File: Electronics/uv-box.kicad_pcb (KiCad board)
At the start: 2 copper layers, 172.7 x 50.8 mm, 73 parts, among them P1 CONN_2

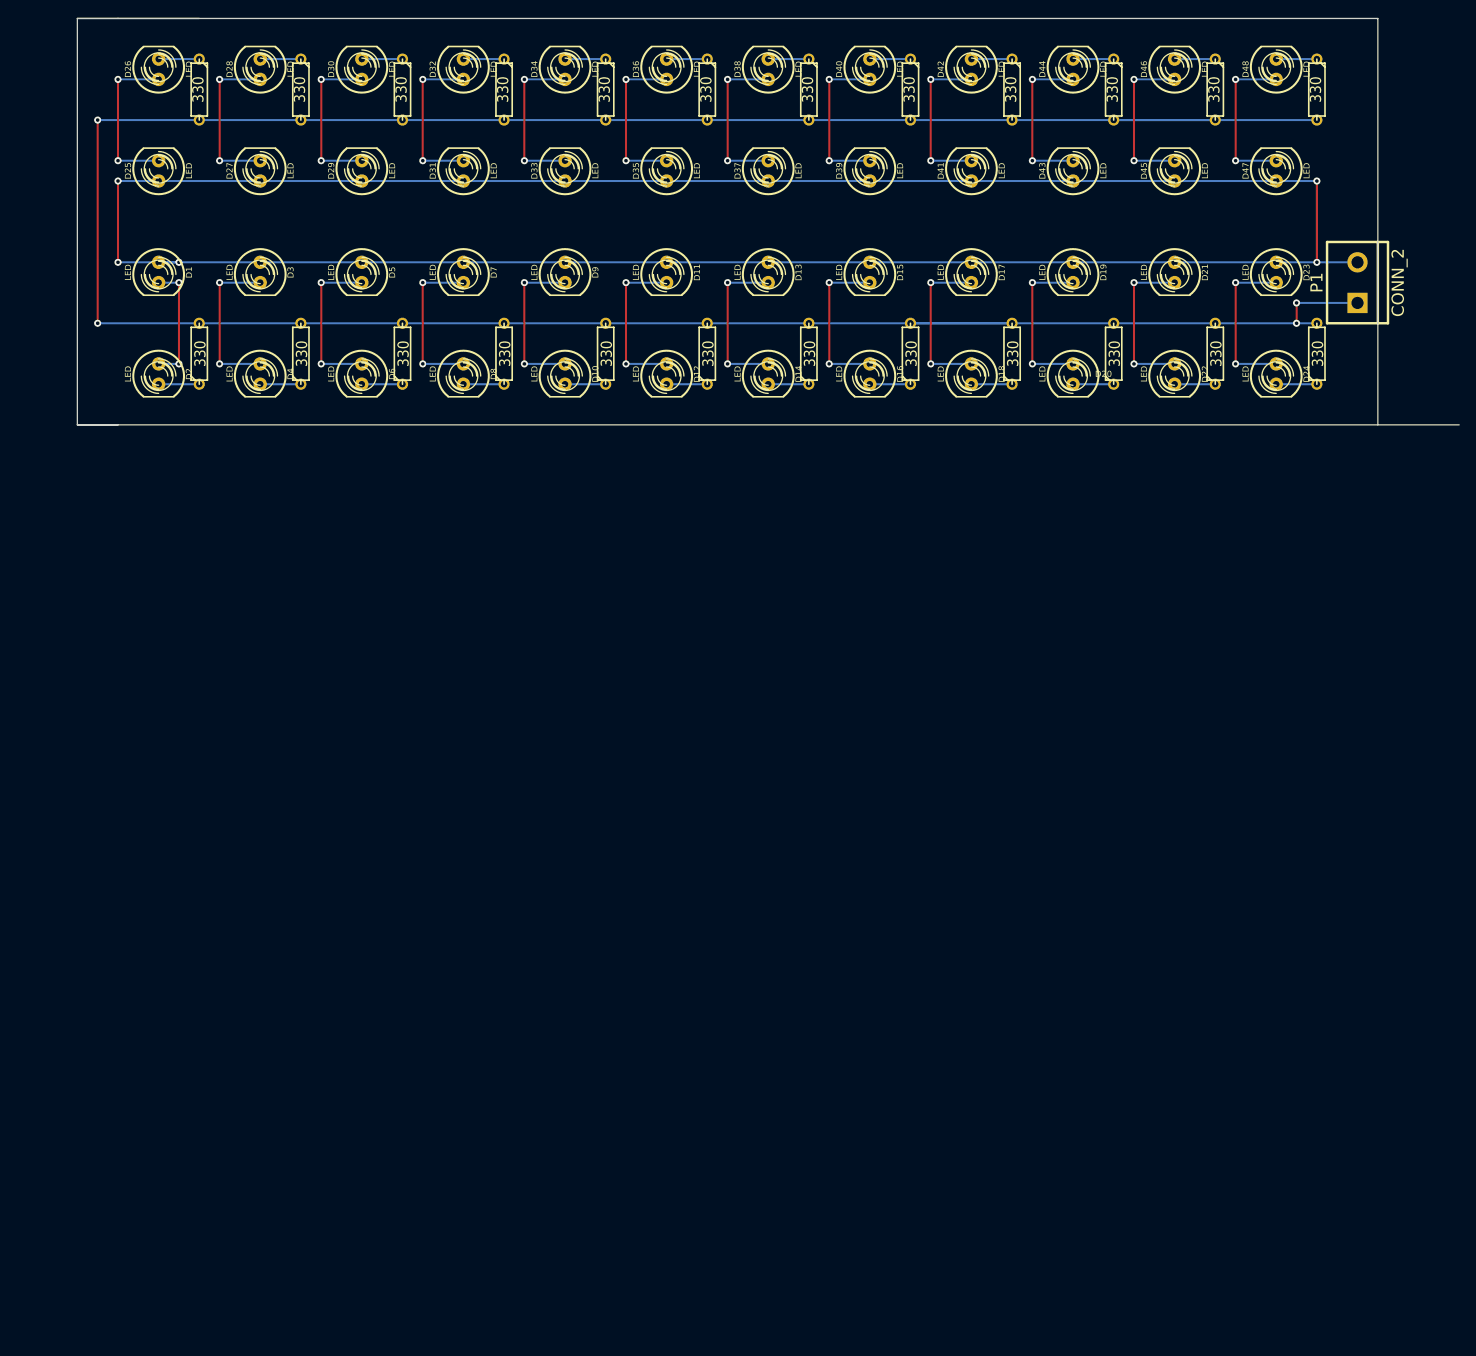
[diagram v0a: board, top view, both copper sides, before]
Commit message: 84 LED per panel.
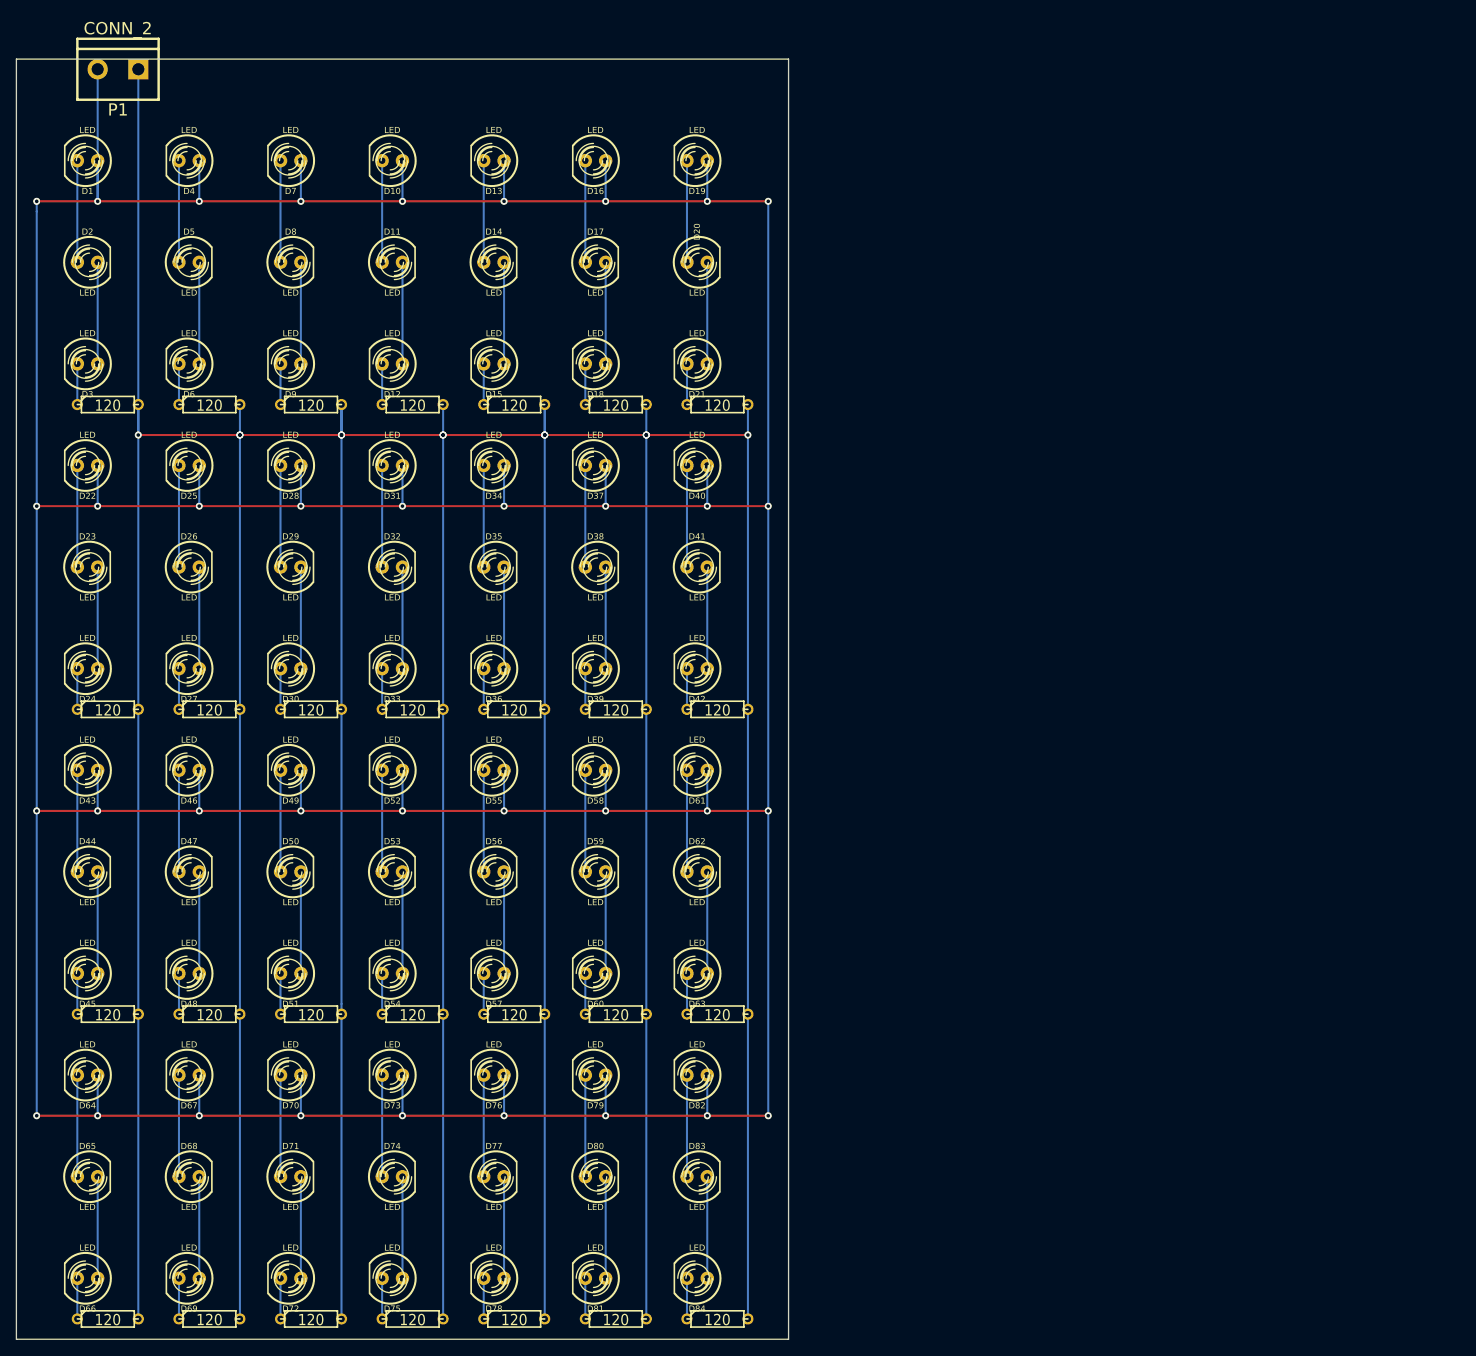
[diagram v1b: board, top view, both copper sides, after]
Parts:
- added D49: LED, LED-5MM, F.Cu at (123.2, 114.3)
- added D50: LED, LED-5MM, F.Cu at (123.2, 127.0)
- added D51: LED, LED-5MM, F.Cu at (123.2, 139.7)
- added D52: LED, LED-5MM, F.Cu at (135.9, 114.3)
- added D53: LED, LED-5MM, F.Cu at (135.9, 127.0)
- added D54: LED, LED-5MM, F.Cu at (135.9, 139.7)
- added D55: LED, LED-5MM, F.Cu at (148.6, 114.3)
- added D56: LED, LED-5MM, F.Cu at (148.6, 127.0)
- added D57: LED, LED-5MM, F.Cu at (148.6, 139.7)
- added D58: LED, LED-5MM, F.Cu at (161.3, 114.3)
- added D59: LED, LED-5MM, F.Cu at (161.3, 127.0)
- added D60: LED, LED-5MM, F.Cu at (161.3, 139.7)
- added D61: LED, LED-5MM, F.Cu at (174.0, 114.3)
- added D62: LED, LED-5MM, F.Cu at (174.0, 127.0)
- added D63: LED, LED-5MM, F.Cu at (174.0, 139.7)
- added D64: LED, LED-5MM, F.Cu at (97.8, 152.4)
- added D65: LED, LED-5MM, F.Cu at (97.8, 165.1)
- added D66: LED, LED-5MM, F.Cu at (97.8, 177.8)
- added D67: LED, LED-5MM, F.Cu at (110.5, 152.4)
- added D68: LED, LED-5MM, F.Cu at (110.5, 165.1)
- added D69: LED, LED-5MM, F.Cu at (110.5, 177.8)
- added D70: LED, LED-5MM, F.Cu at (123.2, 152.4)
- added D71: LED, LED-5MM, F.Cu at (123.2, 165.1)
- added D72: LED, LED-5MM, F.Cu at (123.2, 177.8)
- added D73: LED, LED-5MM, F.Cu at (135.9, 152.4)
- added D74: LED, LED-5MM, F.Cu at (135.9, 165.1)
- added D75: LED, LED-5MM, F.Cu at (135.9, 177.8)
- added D76: LED, LED-5MM, F.Cu at (148.6, 152.4)
- added D77: LED, LED-5MM, F.Cu at (148.6, 165.1)
- added D78: LED, LED-5MM, F.Cu at (148.6, 177.8)
- added D79: LED, LED-5MM, F.Cu at (161.3, 152.4)
- added D80: LED, LED-5MM, F.Cu at (161.3, 165.1)
- added D81: LED, LED-5MM, F.Cu at (161.3, 177.8)
- added D82: LED, LED-5MM, F.Cu at (174.0, 152.4)
- added D83: LED, LED-5MM, F.Cu at (174.0, 165.1)
- added D84: LED, LED-5MM, F.Cu at (174.0, 177.8)
- added R25: 120, R3, F.Cu at (138.4, 182.9)
- added R26: 120, R3, F.Cu at (151.1, 182.9)
- added R27: 120, R3, F.Cu at (163.8, 182.9)
- added R28: 120, R3, F.Cu at (176.5, 182.9)
- R1, R10, R11, R12, R13, R14, R15, R16, R17, R18, R19, R2, R20, R21, R22, R23, R24, R3, R4, R5, R6, R7, R8, R9: value 330 -> 120
- moved R22 198.6 mm to (100.3, 182.9), turned to 0 degrees
- moved R23 198.6 mm to (113.0, 182.9), turned to 0 degrees
- moved R24 198.6 mm to (125.7, 182.9), turned to 0 degrees
- moved D48 176.8 mm to (110.5, 139.7), turned to 180 degrees
- moved D45 168.9 mm to (97.8, 139.7), turned to 180 degrees
- moved D47 161.7 mm to (110.5, 127.0), turned to 0 degrees
- moved D44 158.9 mm to (97.8, 127.0), turned to 0 degrees
- moved P1 157.2 mm to (101.6, 26.7), turned to 180 degrees
- moved D23 153.1 mm to (97.8, 88.9), turned to 0 degrees
- moved D24 153.1 mm to (97.8, 101.6), turned to 180 degrees
- moved D46 151.2 mm to (110.5, 114.3), turned to 180 degrees
- moved D43 144.2 mm to (97.8, 114.3), turned to 180 degrees
- moved D22 136.4 mm to (97.8, 76.2), turned to 180 degrees
- moved R15 121.3 mm to (100.3, 144.8), turned to 0 degrees
- moved R16 121.3 mm to (113.0, 144.8), turned to 0 degrees
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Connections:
- D10 pad 1: N-0000022 -> +12V
- D10 pad 2: N-000009 -> N-0000056
- D11 pad 1: +12V -> N-0000056
- D12 pad 2: N-000008 (its old number) -> N-0000054
- D14 pad 2: N-000007 -> N-0000058
- D15 pad 1: +12V -> N-0000058
- D15 pad 2: N-0000019 -> N-0000057
- D16 pad 1: N-0000019 -> +12V
- D16 pad 2: N-000006 -> N-0000062
- D17 pad 1: +12V -> N-0000062
- D18 pad 2: N-000005 -> N-0000060
- D2 pad 2: N-0000012 -> N-0000045
- D20 pad 2: N-000004 -> N-0000064
- D21 pad 1: +12V -> N-0000064
- D21 pad 2: N-0000016 -> N-0000063
- D22 pad 1: N-0000016 -> +12V
- D22 pad 2: N-000003 -> N-0000069
- D23 pad 1: +12V -> N-0000069
- D24 pad 2: N-000002 -> N-0000067
- D25 pad 1: N-0000041 -> +12V
- D26 pad 2: N-0000038 -> N-0000071
- D27 pad 1: N-0000041 -> N-0000071
- D27 pad 2: N-0000051 -> N-0000070
- D28 pad 1: N-0000051 -> +12V
- D28 pad 2: N-0000037 -> N-0000065
- D29 pad 1: N-0000041 -> N-0000065
- D3 pad 1: +12V -> N-0000045
- D3 pad 2: N-0000025 -> N-0000044
- D30 pad 2: N-0000036 -> N-0000073
- D31 pad 1: N-0000041 -> +12V
- D32 pad 2: N-0000035 -> N-0000077
- D33 pad 1: N-0000041 -> N-0000077
- D33 pad 2: N-0000040 -> N-0000076
- D34 pad 1: N-0000040 -> +12V
- D34 pad 2: N-0000034 -> N-0000081
- D35 pad 1: N-0000041 -> N-0000081
- D36 pad 2: N-0000033 -> N-0000079
- D37 pad 1: N-0000041 -> +12V
- D38 pad 2: N-0000032 -> N-0000083
- D39 pad 1: N-0000041 -> N-0000083
- D39 pad 2: N-0000046 -> N-0000082
- D4 pad 1: N-0000025 -> +12V
- D4 pad 2: N-0000011 -> N-0000050
- D40 pad 1: N-0000046 -> +12V
- D40 pad 2: N-0000031 -> N-0000066
- D41 pad 1: N-0000041 -> N-0000066
- D42 pad 2: N-0000027 -> N-0000085
- D43 pad 1: N-0000041 -> +12V
- D44 pad 2: N-0000030 -> N-000007
- D45 pad 1: N-0000041 -> N-000007
- D45 pad 2: N-0000043 (its old number) -> N-000006
- D46 pad 1: N-0000043 (its old number) -> +12V
- D46 pad 2: N-0000029 -> N-000001
- D47 pad 1: N-0000041 -> N-000001
- D48 pad 2: N-0000028 -> N-000009
- D5 pad 1: +12V -> N-0000050
- D6 pad 2: N-000001 -> N-0000048
- D8 pad 2: N-0000010 (its old number) -> N-0000052
- D9 pad 1: +12V -> N-0000052
- D9 pad 2: N-0000022 -> N-0000051
- R1 pad 1: N-0000012 -> N-0000044
- R10 pad 1: N-000004 -> N-0000073
- R11 pad 1: N-000003 -> N-0000076
- R12 pad 1: N-000002 -> N-0000079
- R13 pad 1: N-0000038 -> N-0000082
- R13 pad 2: N-0000039 -> GND
- R14 pad 1: N-0000037 -> N-0000085
- R14 pad 2: N-0000039 -> GND
- R15 pad 1: N-0000036 -> N-000006
- R15 pad 2: N-0000039 -> GND
- R16 pad 1: N-0000035 -> N-000009
- R16 pad 2: N-0000039 -> GND
- R17 pad 1: N-0000034 -> N-0000012
- R17 pad 2: N-0000039 -> GND
- R18 pad 1: N-0000033 -> N-0000015
- R18 pad 2: N-0000039 -> GND
- R19 pad 1: N-0000032 -> N-0000018
- R19 pad 2: N-0000039 -> GND
- R2 pad 1: N-0000011 -> N-0000048
- R20 pad 1: N-0000031 -> N-0000021
- R20 pad 2: N-0000039 -> GND
- R21 pad 1: N-0000027 -> N-000003
- R21 pad 2: N-0000039 -> GND
- R22 pad 1: N-0000030 -> N-0000031
- R22 pad 2: N-0000039 -> GND
- R23 pad 1: N-0000029 -> N-0000034
- R23 pad 2: N-0000039 -> GND
- R24 pad 1: N-0000028 -> N-0000037
- R24 pad 2: N-0000039 -> GND
- R3 pad 1: N-000001 -> N-0000051
- R4 pad 1: N-0000010 (its old number) -> N-0000054
- R5 pad 1: N-000009 -> N-0000057
- R6 pad 1: N-000008 (its old number) -> N-0000060
- R7 pad 1: N-000007 -> N-0000063
- R8 pad 1: N-000006 -> N-0000067
- R9 pad 1: N-000005 -> N-0000070
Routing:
- net GND: track 200.7 -> 929.6 mm, vias 4 -> 12
- net +12V: track 177.8 -> 753.1 mm, vias 5 -> 36
- net N-0000039: track 165.1 -> 12.7 mm
- net N-0000041: track 149.9 -> 12.7 mm
- net N-0000046: track 20.3 -> 0.00 mm, vias 2 -> 0
- net N-0000043 (its old number): track 20.3 -> 0.00 mm, vias 2 -> 0
- net N-0000025: track 20.3 -> 5.08 mm, vias 2 -> 0
- net N-0000051: track 20.3 -> 5.08 mm, vias 2 -> 0
- net N-0000040: track 20.3 -> 5.08 mm, vias 2 -> 0
- net N-0000026: track 0.00 -> 12.7 mm
- net N-0000081: track 0.00 -> 12.7 mm
- net N-0000069: track 0.00 -> 12.7 mm
- net N-0000066: track 0.00 -> 12.7 mm
- net N-0000065: track 0.00 -> 12.7 mm
- net N-0000064: track 0.00 -> 12.7 mm
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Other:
- board size 172.7 x 50.8 mm -> 96.5 x 160 mm
- net class VeroTrack added: clearance 0.5, trace_width 0.5, via_dia 0.889, via_drill 0.635
